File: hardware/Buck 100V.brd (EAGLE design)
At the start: 22.5 x 55.2 mm, 31 parts, among them M1 SI3430DV, M2 SI5435BDC, Q1 FMMT625, Q2 FMMT723, U1 LT3756EMSE

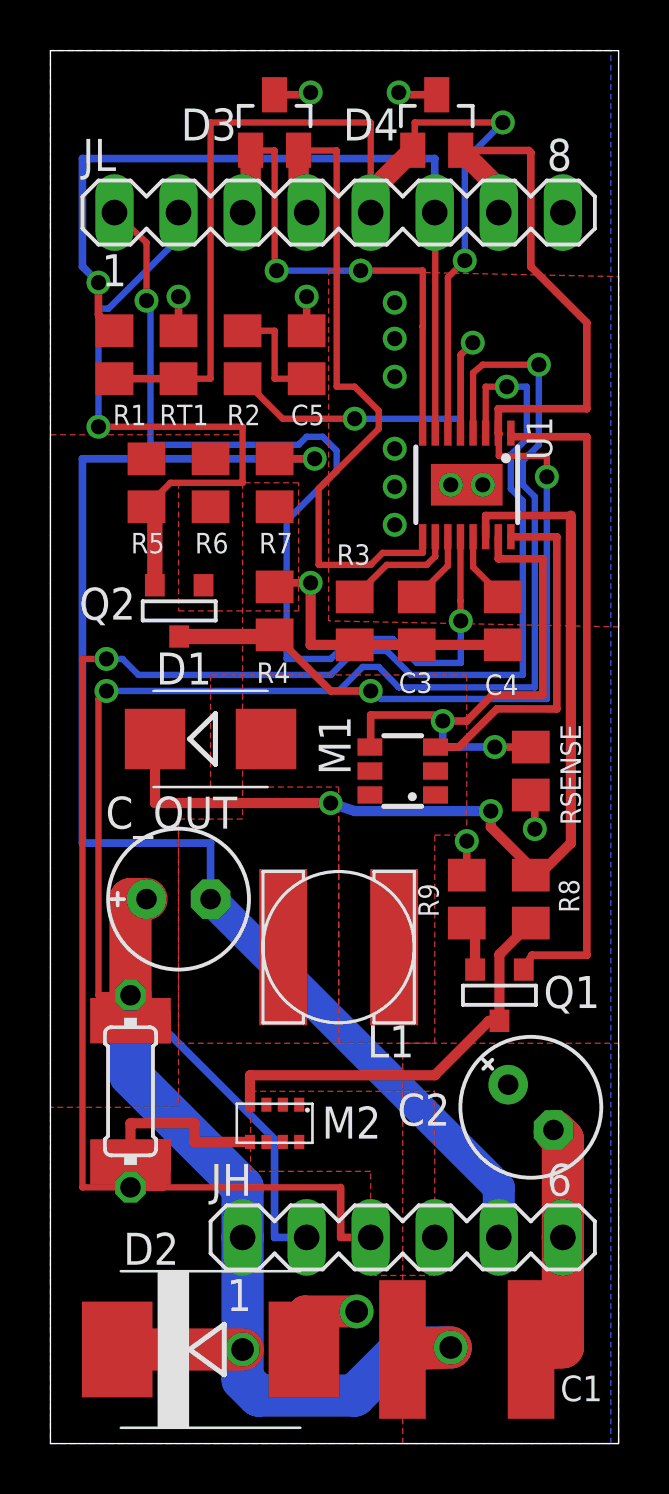
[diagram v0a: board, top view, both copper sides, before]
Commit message: Fine tune routing after reviewing gerbers.
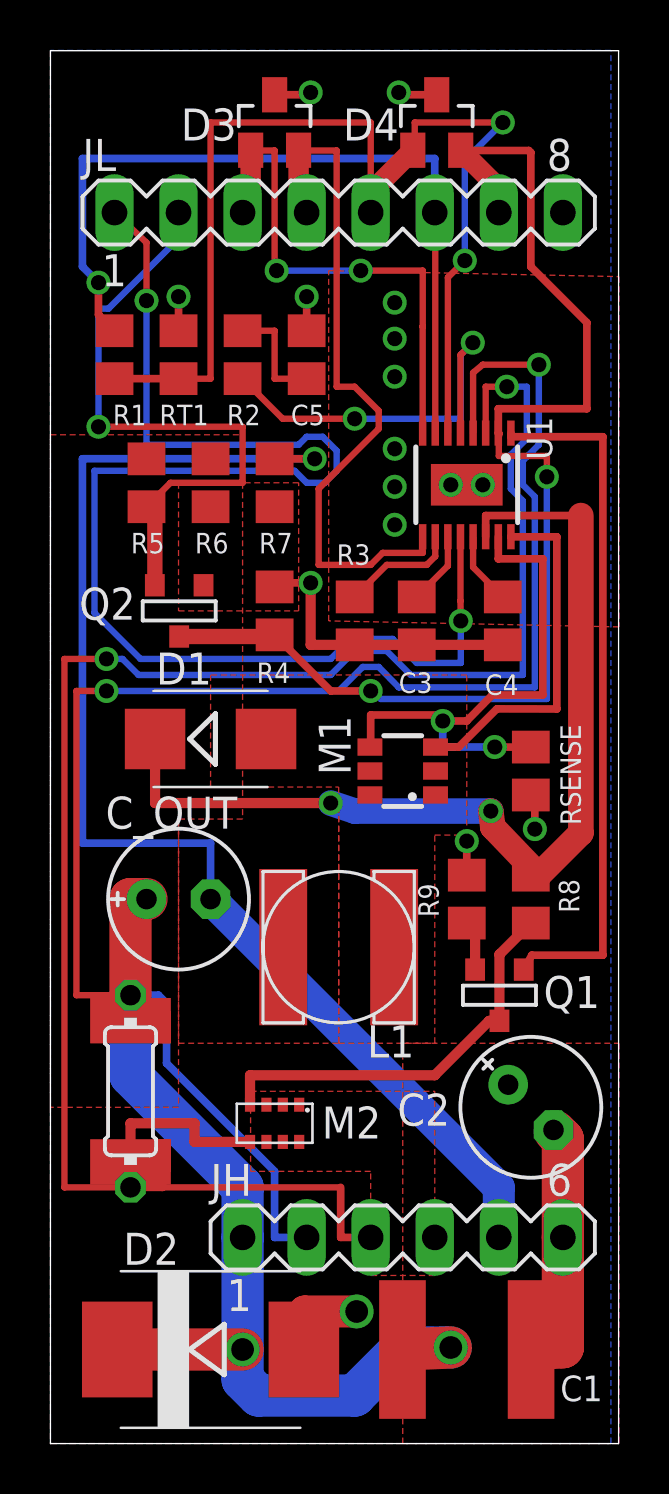
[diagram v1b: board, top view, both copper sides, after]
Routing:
- net SHDN: track 39.3 -> 55.1 mm
- net ISP: track 64.6 -> 67.2 mm
- net ISN: track 70.8 -> 72.2 mm
- net N$11: track 26.6 -> 27.8 mm
- net V+: track 77.3 -> 77.8 mm
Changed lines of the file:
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@@
 <wire x1="3.175" y1="17.78" x2="3.175" y2="16.77" width="0.3048" layer="1"/>
 <wire x1="19.05" y1="22.54" x2="19.365" y2="22.54" width="0.3048" layer="1"/>
-<wire x1="20.6375" y1="23.8125" x2="20.6375" y2="36.801425" width="0.4064" layer="1"/>
-<wire x1="20.6375" y1="36.801425" x2="17.26" y2="36.801425" width="0.3048" layer="1"/>
+<wire x1="21.034375" y1="24.209375" x2="21.034375" y2="36.801425" width="1.016" layer="1"/>
+<wire x1="21.034375" y1="36.801425" x2="17.26" y2="36.801425" width="0.3048" layer="1"/>
 <wire x1="17.26" y1="36.801425" x2="17.26" y2="35.960625" width="0.3048" layer="1"/>
 <wire x1="19.365" y1="22.54" x2="19.365" y2="22.545" width="0.4064" layer="1"/>
-<wire x1="19.365" y1="22.545" x2="17.4625" y2="24.4475" width="0.4064" layer="1"/>
-<wire x1="17.4625" y1="24.4475" x2="17.4625" y2="25.0825" width="0.4064" layer="1"/>
+<wire x1="19.365" y1="22.545" x2="17.541875" y2="24.4475" width="1.016" layer="1"/>
+<wire x1="17.541875" y1="24.4475" x2="17.4625" y2="25.0825" width="1.016" layer="1"/>
 <via x="17.4625" y="25.0825" extent="1-16" drill="0.6"/>
-<wire x1="17.4625" y1="25.0825" x2="12.065" y2="25.0825" width="0.4064" layer="16"/>
-<wire x1="12.065" y1="25.0825" x2="11.1125" y2="25.4" width="0.4064" layer="16"/>
+<wire x1="17.4625" y1="25.0825" x2="12.065" y2="25.0825" width="1.016" layer="16"/>
+<wire x1="12.065" y1="25.0825" x2="11.1125" y2="25.4" width="1.016" layer="16"/>
 <via x="11.1125" y="25.4" extent="1-16" drill="0.6"/>
 <wire x1="11.1125" y1="25.4" x2="4.15" y2="25.4" width="0.4064" layer="1"/>
 <wire x1="4.15" y1="25.4" x2="4.15" y2="27.94" width="0.4064" layer="1"/>
-<wire x1="19.365" y1="22.54" x2="20.6375" y2="23.8125" width="0.4064" layer="1"/>
+<wire x1="19.365" y1="22.54" x2="21.034375" y2="24.209375" width="1.016" layer="1"/>
 <polygon width="0.254" layer="1" rank="5">
 <vertex x="22.5425" y="15.875"/>
@@
 <wire x1="3.81" y1="47.625" x2="3.81" y2="45.323125" width="0.254" layer="1"/>
 <via x="3.81" y="45.323125" extent="1-16" drill="0.6"/>
-<wire x1="3.81" y1="45.323125" x2="3.96875" y2="45.164375" width="0.254" layer="16"/>
-<wire x1="3.96875" y1="45.164375" x2="3.96875" y2="39.608125" width="0.254" layer="16"/>
-<wire x1="3.96875" y1="39.608125" x2="9.8425" y2="39.608125" width="0.254" layer="16"/>
+<wire x1="3.81" y1="45.323125" x2="3.81" y2="39.608125" width="0.254" layer="16"/>
+<wire x1="3.81" y1="39.608125" x2="9.8425" y2="39.608125" width="0.254" layer="16"/>
 <wire x1="9.8425" y1="39.608125" x2="10.16" y2="39.925625" width="0.254" layer="16"/>
 <wire x1="10.16" y1="39.925625" x2="10.795" y2="39.925625" width="0.254" layer="16"/>
 <wire x1="10.795" y1="39.925625" x2="11.350625" y2="39.37" width="0.254" layer="16"/>
 <wire x1="11.350625" y1="39.37" x2="11.350625" y2="38.57625" width="0.254" layer="16"/>
-<wire x1="11.350625" y1="38.57625" x2="9.36625" y2="36.591875" width="0.254" layer="16"/>
-<wire x1="9.36625" y1="36.591875" x2="9.36625" y2="31.115" width="0.254" layer="16"/>
-<wire x1="9.36625" y1="31.115" x2="11.1125" y2="31.115" width="0.254" layer="16"/>
+<wire x1="11.350625" y1="38.57625" x2="10.874375" y2="38.1" width="0.254" layer="16"/>
+<wire x1="10.874375" y1="38.1" x2="10.16" y2="38.1" width="0.254" layer="16"/>
+<wire x1="10.16" y1="38.1" x2="9.68375" y2="38.57625" width="0.254" layer="16"/>
+<wire x1="9.68375" y1="38.57625" x2="1.74625" y2="38.57625" width="0.254" layer="16"/>
+<wire x1="1.74625" y1="38.57625" x2="1.74625" y2="32.940625" width="0.254" layer="16"/>
+<wire x1="1.74625" y1="32.940625" x2="3.571875" y2="31.115" width="0.254" layer="16"/>
+<wire x1="3.571875" y1="31.115" x2="11.1125" y2="31.115" width="0.254" layer="16"/>
 <wire x1="11.1125" y1="31.115" x2="11.90625" y2="31.90875" width="0.254" layer="16"/>
 <wire x1="11.90625" y1="31.90875" x2="13.573125" y2="31.90875" width="0.254" layer="16"/>
@@
 <contactref element="Q1" pad="3"/>
 <wire x1="18.7706" y1="18.796" x2="19.0881" y2="19.3675" width="0.3048" layer="1"/>
-<wire x1="19.0881" y1="19.3675" x2="21.2725" y2="19.3675" width="0.3048" layer="1"/>
-<wire x1="21.2725" y1="19.3675" x2="21.2725" y2="39.925625" width="0.3048" layer="1"/>
-<wire x1="21.2725" y1="39.925625" x2="18.26" y2="39.925625" width="0.3048" layer="1"/>
+<wire x1="19.0881" y1="19.3675" x2="21.9075" y2="19.3675" width="0.3048" layer="1"/>
+<wire x1="21.9075" y1="19.3675" x2="21.9075" y2="39.925625" width="0.3048" layer="1"/>
+<wire x1="21.9075" y1="39.925625" x2="18.26" y2="39.925625" width="0.3048" layer="1"/>
 <wire x1="18.26" y1="39.925625" x2="18.26" y2="40.070625" width="0.3048" layer="1"/>
 </signal>
@@
 <contactref element="JH" pad="2"/>
 <wire x1="10.16" y1="8.175625" x2="8.89" y2="8.175625" width="0.3048" layer="16"/>
-<wire x1="8.89" y1="8.175625" x2="8.89" y2="12.065" width="0.3048" layer="16"/>
-<wire x1="8.89" y1="12.065" x2="3.175" y2="17.78" width="0.3048" layer="16"/>
+<wire x1="8.89" y1="8.175625" x2="8.89" y2="10.795" width="0.3048" layer="16"/>
+<wire x1="8.89" y1="10.795" x2="4.60375" y2="15.08125" width="0.3048" layer="16"/>
+<wire x1="4.60375" y1="15.08125" x2="4.60375" y2="17.4625" width="0.3048" layer="16"/>
+<wire x1="4.60375" y1="17.4625" x2="4.28625" y2="17.78" width="0.3048" layer="16"/>
+<wire x1="4.28625" y1="17.78" x2="3.175" y2="17.78" width="0.3048" layer="16"/>
 <wire x1="4.445" y1="16.51" x2="3.175" y2="17.78" width="0.3048" layer="1"/>
-<wire x1="3.175" y1="17.78" x2="1.905" y2="17.78" width="0.254" layer="1"/>
-<wire x1="1.905" y1="17.78" x2="1.905" y2="29.5275" width="0.254" layer="1"/>
-<wire x1="1.905" y1="29.5275" x2="2.2225" y2="29.845" width="0.254" layer="1"/>
+<wire x1="3.175" y1="17.78" x2="1.031875" y2="17.78" width="0.254" layer="1"/>
+<wire x1="1.031875" y1="17.78" x2="1.031875" y2="29.845" width="0.254" layer="1"/>
+<wire x1="1.031875" y1="29.845" x2="2.2225" y2="29.845" width="0.254" layer="1"/>
 <via x="2.2225" y="29.845" extent="1-16" drill="0.6"/>
 <wire x1="2.2225" y1="29.845" x2="11.43" y2="29.845" width="0.254" layer="16"/>
@@
 <wire x1="3.175" y1="10.16" x2="4.445" y2="10.16" width="0.3048" layer="1"/>
 <wire x1="4.445" y1="10.16" x2="4.445" y2="11.43" width="0.3048" layer="1"/>
-<wire x1="3.175" y1="10.16" x2="1.27" y2="10.16" width="0.254" layer="1"/>
-<wire x1="1.27" y1="10.16" x2="1.27" y2="31.115" width="0.254" layer="1"/>
-<wire x1="1.27" y1="31.115" x2="2.2225" y2="31.115" width="0.254" layer="1"/>
+<wire x1="3.175" y1="10.16" x2="0.555625" y2="10.16" width="0.254" layer="1"/>
+<wire x1="0.555625" y1="10.16" x2="0.555625" y2="31.115" width="0.254" layer="1"/>
+<wire x1="0.555625" y1="31.115" x2="2.2225" y2="31.115" width="0.254" layer="1"/>
 <via x="2.2225" y="31.115" extent="1-16" drill="0.6"/>
 <wire x1="3.175" y1="10.16" x2="11.509375" y2="10.16" width="0.254" layer="1"/>

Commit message: Add BatchPCB design rules and cam script. Make some adjustments to the layout for batchPCB rule check.
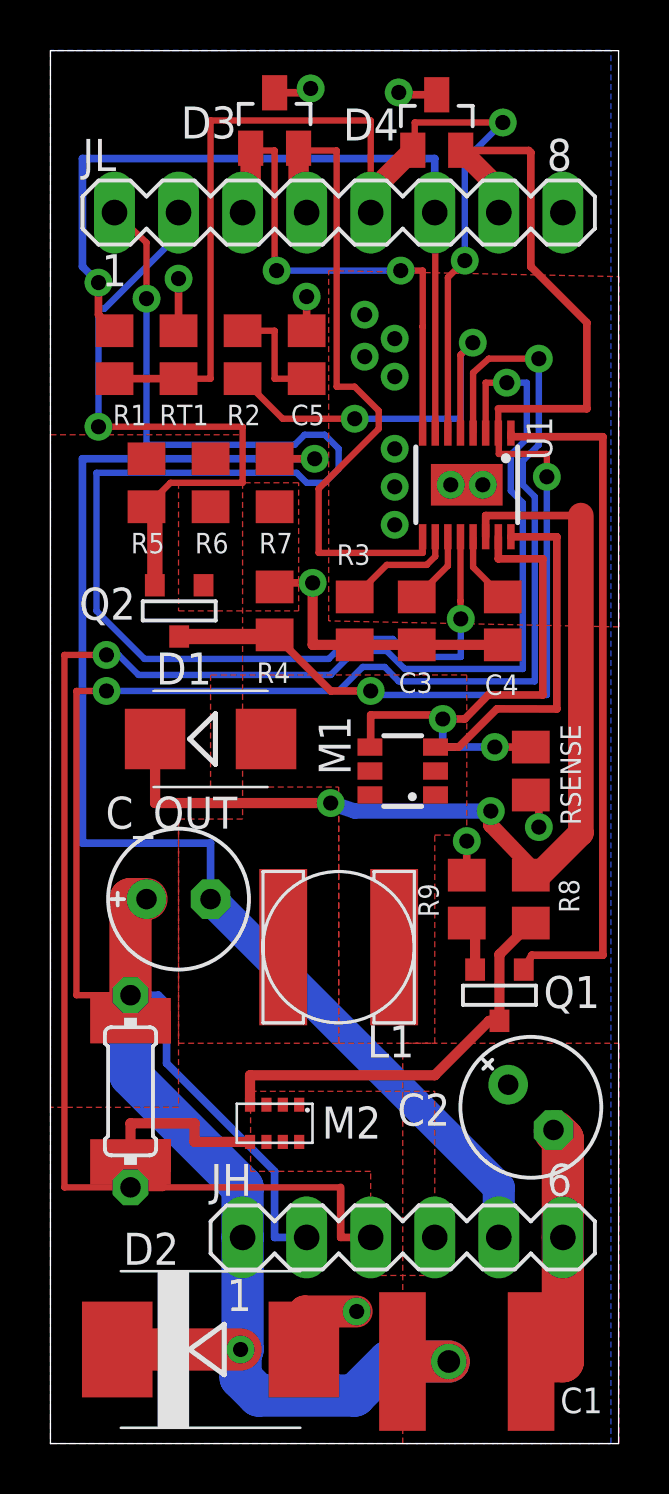
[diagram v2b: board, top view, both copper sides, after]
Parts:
- moved C1 0.48 mm to (16.5, 3.25)
- moved D3 0.08 mm to (8.89, 52.5)
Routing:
- net GND: track 34.4 -> 35.8 mm, vias 16 -> 17
- net /OPEN_LED: track 27.8 -> 27.2 mm
